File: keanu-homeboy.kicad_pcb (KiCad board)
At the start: 2 copper layers, 64.6 x 98.8 mm, 13 parts, among them X1 Badgelife_sao_connector_v169b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

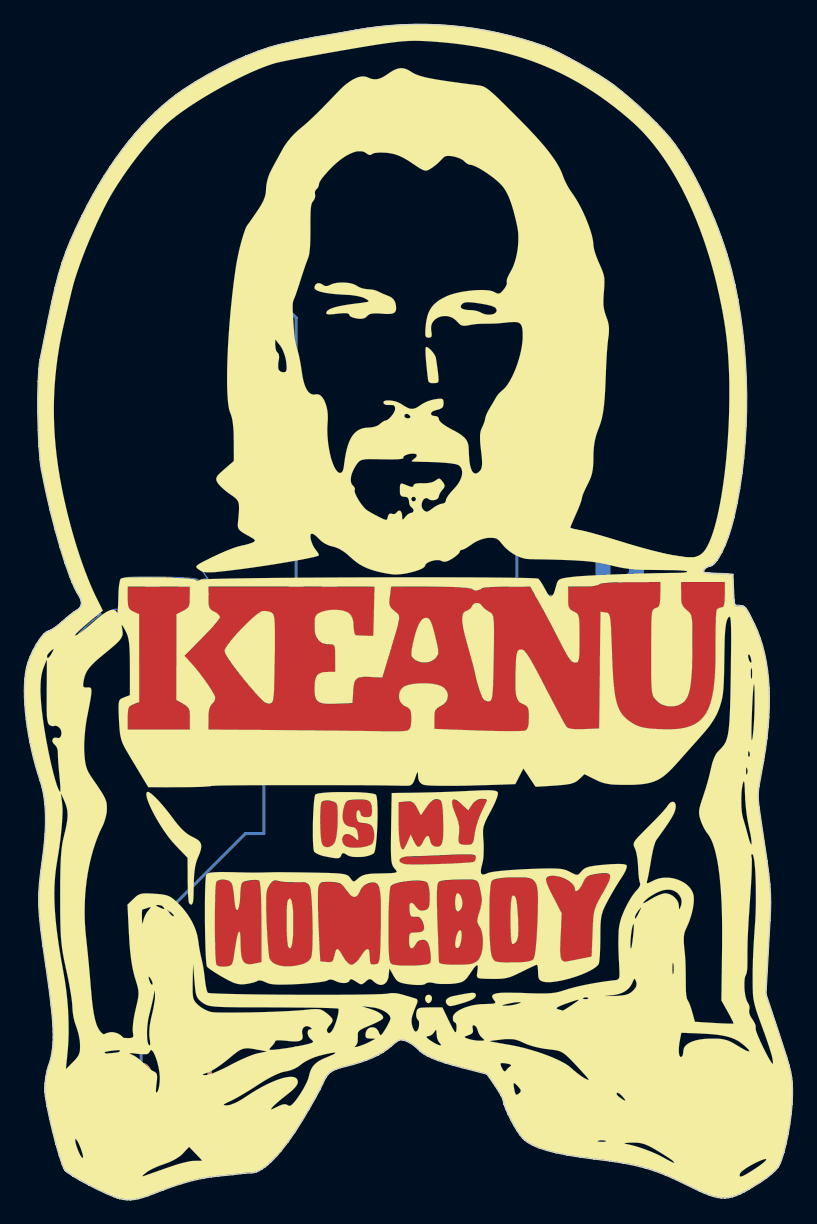
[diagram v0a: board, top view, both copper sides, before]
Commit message: added pin version
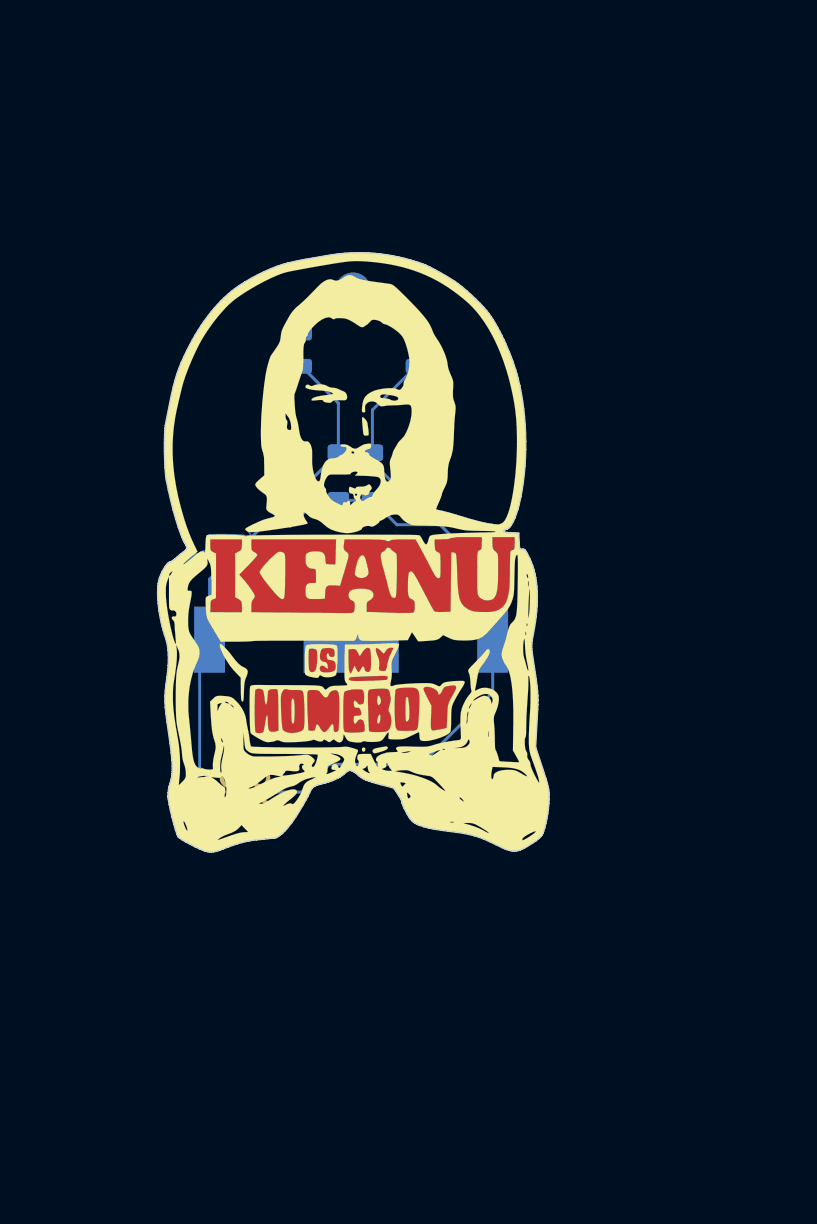
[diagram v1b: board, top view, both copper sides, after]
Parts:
- removed the G*** at (0.00, 0.00) (x6)
- added ?: TestPoint_Pad_D3.0mm, TestPoint:TestPoint_Pad_D3.0mm, B.Cu at (-4.66, -27.1)
- added BT1: Battery_Cell, Battery:BatteryHolder_MPD_BC2003_1x2032, B.Cu at (-4.82, 2.32)
- added G*** (x6): LOGO, LOGO, F.Cu at (0.00, 0.00)
- R1: footprint Resistor_SMD:R_1206_3216Metric -> Resistor_SMD:R_1806_4516Metric
- moved X1 25.3 mm to (-15.1, 15.2)
- moved D3 25.0 mm to (0.64, -22.1), turned to 270 degrees
- moved D2 23.5 mm to (-8.99, -22.1), turned to 270 degrees
- moved D4 20.6 mm to (1.05, -11.4)
- moved D1 17.8 mm to (-9.82, -11.4)
- moved R2 14.2 mm to (-3.03, -11.4), turned to 270 degrees
- moved R1 10.1 mm to (-5.89, -11.4), turned to 270 degrees
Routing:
- net /VDD: track 59.5 -> 86.7 mm
- net Net-(D3-Pad2): track 37.5 -> 14.7 mm
- net Net-(D1-Pad2): track 36.7 -> 13.9 mm
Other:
- board size 64.6 x 98.8 mm -> 32.9 x 50.4 mm

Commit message: updates for production
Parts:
- removed the G*** at (0.00, 0.00) (x6)
- added G*** (x6): LOGO, LOGO, F.Cu at (144.3, 100.1)
- D1, D2, D3, D4: footprint LED_SMD:LED_1206_3216Metric -> BadgePiratesFootprint:QBLP615
- R1, R2: footprint Resistor_SMD:R_1806_4516Metric -> Resistor_SMD:R_0805_2012Metric_Pad1.20x1.40mm_HandSolder
- X1: footprint my-ki-cad-parts:Badgelife-SAOv169-SAO-2x3 -> BadgePirateFootprints:Badgelife-SAOv169-SAO_Side_B.SLK
- moved D3 178.1 mm to (147.8, 78.2), turned to 90 degrees
- moved D4 177.8 mm to (148.1, 88.5), turned to 90 degrees
- moved ? 175.6 mm to (139.6, 73.0)
- moved BT1 175.6 mm to (139.5, 102.4)
- moved R1 175.6 mm to (138.4, 88.7)
- moved R2 175.6 mm to (141.2, 88.7)
- moved X1 175.6 mm to (129.2, 115.3)
- moved D2 173.7 mm to (132.5, 78.6)
- moved D1 172.6 mm to (131.1, 88.4)
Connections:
- X1 pad 3: Net-(X1-Pad3) -> unconnected-(X1-SDA-Pad3)
- X1 pad 4: Net-(X1-Pad4) -> unconnected-(X1-SCL-Pad4)
- X1 pad 5: Net-(X1-Pad5) -> unconnected-(X1-GPIO1-Pad5)
- X1 pad 6: Net-(X1-Pad6) -> unconnected-(X1-GPIO2-Pad6)
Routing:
- net /VDD: track 86.7 -> 56.5 mm
- net Net-(D1-A): track 13.9 -> 15.7 mm
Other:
- net class Default removed
